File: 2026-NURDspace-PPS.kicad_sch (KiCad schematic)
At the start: 4 parts

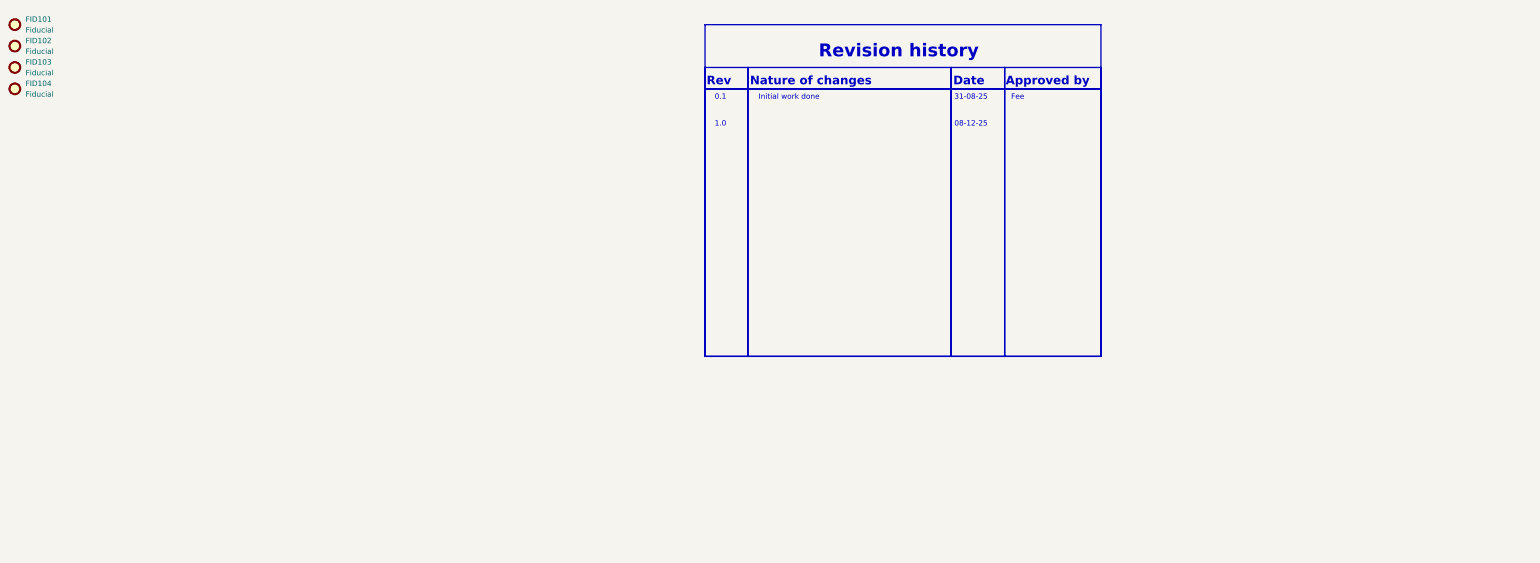
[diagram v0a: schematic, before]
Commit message: Started on gathering parts
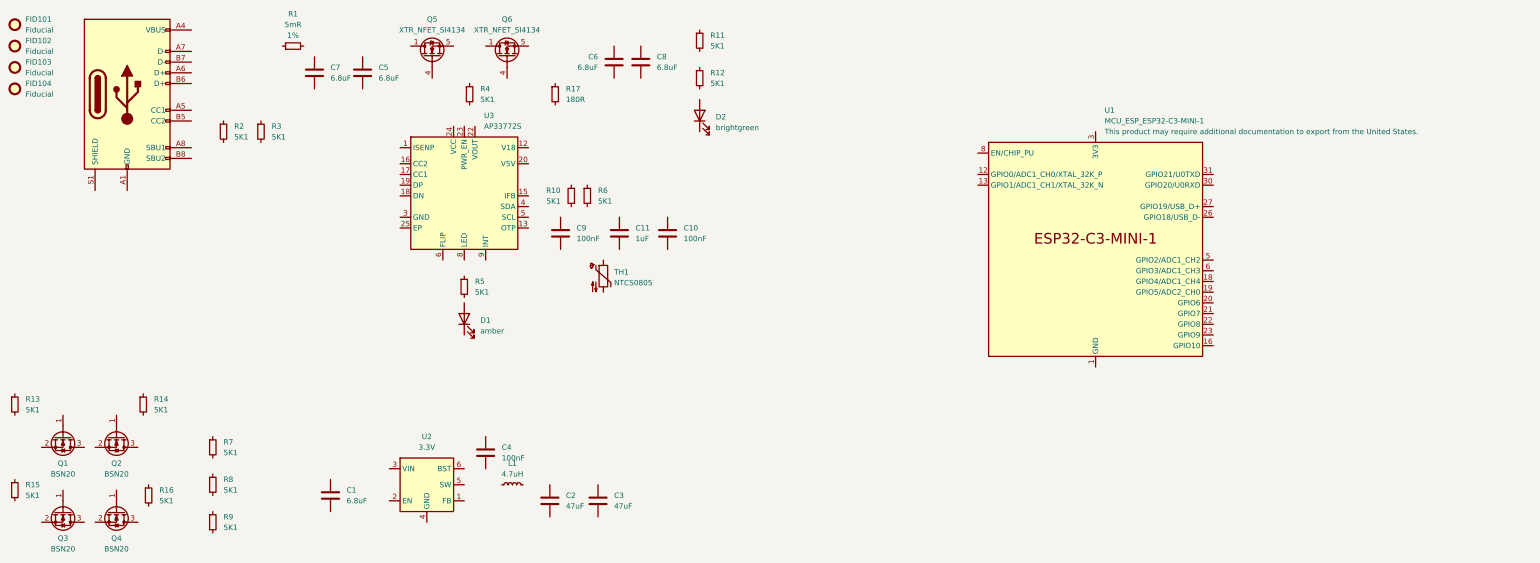
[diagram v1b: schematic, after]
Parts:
- added C1, C5, C6, C7, C8: 6.8uF, Capacitor_SMD:C_1206_3216Metric, symbol 0_NRD_Capacitors_MLCC:CB_＋＝_1206B685K500CT
- added C10, C4, C9: 100nF, Capacitor_SMD:C_0805_2012Metric, symbol 0_NRD_Capacitors_MLCC:C8_＊％_0805B104K500CT
- added C11: 1uF, Capacitor_SMD:C_1206_3216Metric, symbol 0_NRD_Capacitors_MLCC:CB_＋＃_1206B105K250CT
- added C2, C3: 47uF, Capacitor_SMD:C_1210_3225Metric, symbol 00_projectlib:CB_＝！_MAASL32MSB7476MPNA01
- added D1: amber, LED_SMD:LED_0603_1608Metric, symbol 0_NRD_Leds_and_Opto:LED_WRTH_150060AS75000
- added D2: brightgreen, LED_SMD:LED_0603_1608Metric, symbol 0_NRD_Leds_and_Opto:LED_WRTH_150060VS75000
- added J1: UJ20-C-H-C-4-SMT-TR, 0_NRD_footprints:USB_C_Receptacle_SSKY_UJ20-C-H-C-4-SMT-TR, symbol 0_NRD_Connectors:USB_SSKY_UJ20-C-H-C-4-SMT-TR
- added L1: 4.7uH, 0_NRD_footprints:FB_2020_5650Metric, symbol 00_projectlib:IND_VSHY_IMC2220ER4R7K
- added Q1, Q2, Q3, Q4: BSN20, Package_TO_SOT_SMD:SOT-23, symbol 00_projectlib:XTR_NFET_BSN20
- added Q5, Q6: XTR_NFET_SI4134, Package_SO:SOIC-8_3.9x4.9mm_P1.27mm, symbol 00_projectlib:XTR_NFET_SI4134
- added R1: 5mR, Resistor_SMD:R_1206_3216Metric, symbol 00_projectlib:RES_1206_5mR
- added R10, R11, R12, R13, R14, R15, R16, R2, R3, R4, R5, R6, R7, R8, R9: 5K1, Resistor_SMD:R_0805_2012Metric, symbol 0_NRD_Resistors:R_0805_5K1
- added R17: 180R, Resistor_SMD:R_0805_2012Metric, symbol 0_NRD_Resistors:R_0805.ͺ_180R
- added TH1: NTCS0805, Resistor_SMD:R_0805_2012Metric, symbol 00_projectlib:NTC_NTCS0805E3103HHT
- added U1: MCU_ESP_ESP32-C3-MINI-1, 0_NRD_footprints:ESP32-C3-MINI-1U, symbol 0_NRD_Microcontrollers:MCU_ESP_ESP32-C3-MINI-1U
- added U2: 3.3V, Package_TO_SOT_SMD:TSOT-23-6, symbol 00_projectlib:BCK_DIOD_AP63203
- added U3: AP33772S, Package_DFN_QFN:QFN-24-1EP_4x4mm_P0.5mm_EP2.6x2.6mm, symbol 00_projectlib:AP33772S
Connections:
- new net: Q6.1 (S), Q6.2 (S), Q6.3 (S)
- new net: Q6.5 (D), Q6.6 (D), Q6.7 (D), Q6.8 (D)
- new net: U1.1 (GND), U1.11 (GND), U1.14 (GND), U1.2 (GND), U1.36 (GND), U1.37 (GND), U1.38 (GND), U1.39 (GND), U1.40 (GND), U1.41 (GND), U1.42 (GND), U1.43 (GND), U1.44 (GND), U1.45 (GND), U1.46 (GND), U1.47 (GND), U1.48 (GND), U1.49 (GND), U1.50 (GND), U1.51 (GND), U1.52 (GND), U1.53 (GND)
- new net: U3.10 (NC), U3.11 (NC), U3.14 (NC), U3.2 (NC), U3.21 (NC), U3.7 (NC)
- new net: J1.A1 (GND), J1.A12 (GND), J1.B1 (GND), J1.B12 (GND)
- new net: J1.A4 (VBUS), J1.A9 (VBUS), J1.B4 (VBUS), J1.B9 (VBUS)
- new net: Q5.1 (S), Q5.2 (S), Q5.3 (S)
- new net: Q5.5 (D), Q5.6 (D), Q5.7 (D), Q5.8 (D)
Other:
- note removed: "0.1"
- note removed: "08-12-25"
- note removed: "1.0"
- note removed: "31-08-25"
- note removed: "Approved by"
- note removed: "Date"
- note removed: "Fee"
- note removed: "Initial work done"
- note removed: "Nature of changes"
- note removed: "Rev"
- note removed: "Revision history"

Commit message: Added all components
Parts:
- removed C2, C3: 47uF, Capacitor_SMD:C_1210_3225Metric, symbol 00_projectlib:CB_＝！_MAASL32MSB7476MPNA01
- removed L1: 4.7uH, 0_NRD_footprints:FB_2020_5650Metric, symbol 00_projectlib:IND_VSHY_IMC2220ER4R7K
- removed R1: 5mR, Resistor_SMD:R_1206_3216Metric, symbol 00_projectlib:RES_1206_5mR
- removed U1: MCU_ESP_ESP32-C3-MINI-1, 0_NRD_footprints:ESP32-C3-MINI-1U, symbol 0_NRD_Microcontrollers:MCU_ESP_ESP32-C3-MINI-1U
- added C105: 1uF, Capacitor_SMD:C_1206_3216Metric, symbol 0_NRD_Capacitors_MLCC:CB_＋＃_1206B105K250CT
- added C107: 180uF, 0_NRD_footprints:CP_Wurth_WCAP-PHLE-L7.3W4.3H1.9, symbol 00_projectlib:WCAP_WURTH_875035119002
- added C112: 100nF, Capacitor_SMD:C_0805_2012Metric, symbol 0_NRD_Capacitors_MLCC:C8_＊％_0805B104K500CT
- added D101, D102, D103, D104, D105, D106, D107, D108, D110, D111, D112, D113, D114, D115, D116, D117: MXA8-PW40-0000, 0_NRD_footprints:LED_Luxeon3535_3.5x3.7mm, symbol 00_projectlib:LED_LUML_MXA8-PW40-0000
- added D119, D120, D121, D122, D123, D124, D125, D126, D127, D128: Led_0603_superred_generic, LED_SMD:LED_0603_1608Metric, symbol 0_NRD_Leds_and_Opto:LED_WRTH_150060SS75000
- added L101: 4.7uH, Inductor_SMD:L_1008_2520Metric_Pad1.43x2.20mm_HandSolder, symbol 00_projectlib:IND_WRTH_74479889247
- added R105, R106, R107, R108, R109, R110, R111, R112, R117, R118, R119, R120, R123, R124, R125, R126: 39R, Resistor_SMD:R_0805_2012Metric, symbol 0_NRD_Resistors:R_0805.__39R
- added R122: 5mR, Resistor_SMD:R_0805_2012Metric_Pad1.20x1.40mm_HandSolder, symbol 00_projectlib:RES_0805_5mR
- added R132, R133, R134, R135, R136, R139, R140, R141, R142, R143: 270R, Resistor_SMD:R_0805_2012Metric, symbol 0_NRD_Resistors:R_0805.ͺ_270R
- added R144: 5K1, Resistor_SMD:R_0805_2012Metric, symbol 0_NRD_Resistors:R_0805_5K1
- added SW101: 430172085816, 0_NRD_footprints:btn_momentary_430172085816, symbol 0_NRD_User_Inputs:BTN_MTRY_430172085816
- added U101, U102, U103, U104, U105, U106, U108, U109, U113, U114, U115, U116, U118, U119, U121, U122: 1G126, Package_TO_SOT_SMD:SOT-353_SC-70-5, symbol 0_NRD_Level_and_logic:LOG_7400_1G126
- added U107, U112, U117, U120: 74HC595, Package_SO:SOIC-16_3.9x9.9mm_P1.27mm, symbol 0_NRD_Level_and_logic:LOG_7400_595
- added U123: 481RV12172100, 0_NRD_footprints:481RV12172100, symbol 00_projectlib:BTN_ENC_WURTH_481RV12172100
- added U124: ESP32-S3-WROOM-1, 0_NRD_footprints:ESP32-S3-WROOM-1, symbol 0_NRD_Microcontrollers:MCU_ESP_ESP32-S3-WROOM-1
- renumbered C7 to C101, C1 to C102, C5 to C103, C4 to C104, C9 to C106, C6 to C108, C11 to C109, C8 to C110, C10 to C111, D1 to D109, D2 to D118, J1 to J101, Q1 to Q101, Q3 to Q102, Q2 to Q103, Q4 to Q104, Q5 to Q105, Q6 to Q106, R13 to R101, R15 to R102, R14 to R103, R16 to R104, R7 to R113, R8 to R114, R9 to R115, R2 to R116, R3 to R121, R5 to R127, R4 to R128, R17 to R129, R10 to R130, R6 to R131, R11 to R137, R12 to R138, TH1 to TH101, U2 to U110, U3 to U111
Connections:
- new net: U124.1 (GND), U124.40 (GND), U124.41 (GND)
- new net +3.3V: R144.1
- new net ESP_BOOTSEL: C112.1, R144.2, SW101.1, SW101.2
- new net GND: C112.2, SW101.3, SW101.4
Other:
- note added: "3V to 20V indicator"
- note added: "Boot Select"
- note added: "Decimal indicator"
- note added: "Google AN97055"

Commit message: Drawn the schematic
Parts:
- removed D101, D102, D103, D104, D105, D106, D107, D108, D110, D111, D112, D113, D114, D115, D116, D117: MXA8-PW40-0000, 0_NRD_footprints:LED_Luxeon3535_3.5x3.7mm, symbol 00_projectlib:LED_LUML_MXA8-PW40-0000
- removed D119, D120, D121, D122, D123, D124, D125, D126, D127, D128: Led_0603_superred_generic, LED_SMD:LED_0603_1608Metric, symbol 0_NRD_Leds_and_Opto:LED_WRTH_150060SS75000
- removed R105, R106, R107, R108, R109, R110, R111, R112, R117, R118, R119, R120, R123, R124, R125, R126: 39R, Resistor_SMD:R_0805_2012Metric, symbol 0_NRD_Resistors:R_0805.__39R
- removed R113, R114, R130, R131: 5K1, Resistor_SMD:R_0805_2012Metric, symbol 0_NRD_Resistors:R_0805_5K1
- removed R132, R133, R134, R135, R136, R139, R140, R141, R142, R143: 270R, Resistor_SMD:R_0805_2012Metric, symbol 0_NRD_Resistors:R_0805.ͺ_270R
- removed U101, U102, U103, U104, U105, U106, U108, U109, U113, U114, U115, U116, U118, U119, U121, U122: 1G126, Package_TO_SOT_SMD:SOT-353_SC-70-5, symbol 0_NRD_Level_and_logic:LOG_7400_1G126
- removed U107, U112, U117, U120: 74HC595, Package_SO:SOIC-16_3.9x9.9mm_P1.27mm, symbol 0_NRD_Level_and_logic:LOG_7400_595
- added C108, C110, C115: 100nF, Capacitor_SMD:C_0805_2012Metric, symbol 0_NRD_Capacitors_MLCC:C8_＊％_0805B104K500CT
- added R109, R110, R112, R118: 5K1, Resistor_SMD:R_0805_2012Metric, symbol 0_NRD_Resistors:R_0805_5K1
- renumbered C103 to C102, C108 to C103, C110 to C104, C109 to C105, C112 to C107, C111 to C109, C104 to C111, C102 to C112, C105 to C113, C107 to C114, D118 to D101, D109 to D102, Q105 to Q101, Q106 to Q102, Q101 to Q103, Q103 to Q104, Q102 to Q105, Q104 to Q106, R122 to R101, R137 to R102, R138 to R103, R128 to R104, R129 to R105, R116 to R106, R121 to R107, R144 to R108, R127 to R111, R101 to R113, R103 to R114, R102 to R116, R104 to R117, U111 to U101, U124 to U102, U123 to U103, U110 to U104
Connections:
- net +3.3V: now also C113.1, C114.1, L101.2, Q104.1 (G), Q106.1 (G), R114.1, R115.1, R117.1, U102.2 (3V3), U104.1 (FB), C108.1, R109.1, R110.1, R118.1
- net ESP_BOOTSEL: now also U102.27 (GPIO0/BOOT)
- net GND: now also C101.2, C102.2, C103.2, C104.2, C105.2, C106.2, C109.2, C112.2, C113.2, C114.2, D101.1 (K), D102.1 (K), J101.A1 (GND), J101.A12 (GND), J101.B1 (GND), J101.B12 (GND), J101.S1 (SHIELD), R106.2, R107.2, TH101.2, U101.25 (EP), U101.3 (GND), U102.1 (GND), U102.40 (GND), U102.41 (GND), U103.13, U104.4 (GND), C108.2, C110.2, C115.2, R112.2
- net VBUS: now reaches C103.1
- net VBUS: now also C104.1, C112.1, Q102.5 (D), Q102.6 (D), Q102.7 (D), Q102.8 (D), R102.1, R105.1, U104.2 (EN), U104.3 (VIN)
- net at D102.2 (A): now also R111.2
- net at U103.1: now also U102.15 (GPIO3/TOUCH3/ADC1_CH2)
- net at U103.2: now also U102.4 (GPIO4/TOUCH4/ADC1_CH3)
- net at U103.3: now also U102.5 (GPIO5/TOUCH5/ADC1_CH4)
- net at U103.4: now also U102.6 (GPIO6/TOUCH6/ADC1_CH5)
- net at U103.5: now also U102.17 (GPIO9/TOUCH9/ADC1_CH8/FSPIHD/SUBSPIHD)
- net at U103.6: now also U102.18 (GPIO10/TOUCH10/ADC1_CH9/FSPICS0/FSPIIO4/SUBSPICS0)
- net at U103.7: now also U102.19 (GPIO11/TOUCH11/ADC2_CH0/FSPID/FSPIIO5/SUBSPID)
- net at U103.8: now also U102.20 (GPIO12/TOUCH12/ADC2_CH1/FSPICLK/FSPIIO6/SUBSPICLK)
- net at U103.C: now also R115.2, C115.1
- net at R103.1: now also R102.2
- net at R103.2: now also D101.2 (A)
- net at R106.1: now also J101.B5 (CC2), U101.16 (CC2)
- net at U103.12: now also U102.23 (GPIO21), R118.2
- net +5V: now reaches Q105.1 (G)
- net +5V: now also C105.1, Q103.1 (G), R113.1, R116.1, U101.20 (V5V)
- net I^{2}C_{SCL5V}: now reaches Q105.2 (S)
- net I^{2}C_{SCL5V}: now also R116.2, U101.5 (SCL)
- net at Q105.3 (D): now also Q106.2 (S)
- net DATA1: now reaches U102.11 (GPIO18/U1RXD/ADC2_CH7/CLK_OUT3)
- net CLK: now reaches U102.12 (GPIO8/TOUCH8/ADC1_CH7/SUBSPICS1)
- net D-: now reaches U102.13 (GPIO19/U1RTS/ADC2_CH8/CLK_OUT2/USB_D-)
- net D-: now also J101.A7 (D-), J101.B7 (D-)
- net D+: now reaches U102.14 (GPIO20/U1CTS/ADC2_CH9/CLK_OUT1/USB_D+)
- net D+: now also J101.A6 (D+), J101.B6 (D+)
- net at U102.21 (GPIO13/TOUCH13/ADC2_CH2/FSPIQ/FSPIIO7/SUBSPIQ): now also U103.L2
- net at U102.22 (GPIO14/TOUCH14/ADC2_CH3/FSPIWP/FSPIDQS/SUBSPIWP): now also U103.L1
- net at U102.3 (EN): now also C110.1, R109.2
- net I^{2}C_{SCL3V3}: now reaches U102.36 (U0RXD/GPIO44/CLK_OUT2)
- net I^{2}C_{SCL3V3}: now also Q106.3 (D), R117.2
- net I^{2}C_{SDA3V3}: now reaches U102.37 (U0TXD/GPIO43/CLK_OUT1)
- net I^{2}C_{SDA3V3}: now also Q104.2 (S), R114.2
- net OE: now reaches U102.38 (GPIO2/TOUCH2/ADC1_CH1)
- net OE: now also R112.1
- net ~{CLR}: now reaches U102.39 (GPIO1/TOUCH1/ADC1_CH0)
- net ~{CLR}: now also R110.2
- net at R111.1: now also U101.8 (LED)
- net at Q102.1 (S), Q102.2 (S), Q102.3 (S): now also Q101.1 (S), Q101.2 (S), Q101.3 (S)
- net at Q102.4 (G): now also Q101.4 (G), R104.1
- net I^{2}C_{SDA5V}: now reaches Q103.2 (S)
- net I^{2}C_{SDA5V}: now also R113.2, U101.4 (SDA)
- net at Q103.3 (D): now also Q104.3 (D)
- net at R107.1: now also J101.A5 (CC1), U101.17 (CC1)
- net at C106.1: now also U101.12 (V18)
- net at C101.1: now also C102.1, Q101.5 (D), Q101.6 (D), Q101.7 (D), Q101.8 (D), R101.2, U101.24 (VCC)
- net at R105.2: now also U101.22 (VOUT)
- net at R104.2: now also U101.23 (PWR_EN)
- net at L101.1: now also C111.2, U104.5 (SW)
- net at U101.1 (ISENP): now also J101.A4 (VBUS), J101.A9 (VBUS), J101.B4 (VBUS), J101.B9 (VBUS), R101.1
- net at U101.13 (OTP): now also TH101.1
- net at U101.15 (IFB): now also C109.1
- net at C111.1: now also U104.6 (BST)
- no-connect marks 0 -> 6
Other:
- added sheet Output Indicators (Output Indicators.kicad_sch)
- note removed: "3V to 20V indicator"
- note removed: "Decimal indicator"
- moved on the sheet: C101, C102, C103, C104, C105, C106, C107, C109, C111, C112, C113, C114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

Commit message: First version of layout
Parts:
- removed SW101: 430172085816, 0_NRD_footprints:btn_momentary_430172085816, symbol 0_NRD_User_Inputs:BTN_MTRY_430172085816
- added SW101: 430483025816, 0_NRD_footprints:SW_Push_430483025816, symbol 0_NRD_User_Inputs:BTN_MTRY_430483025816
- U102: renamed from U101; footprint Package_DFN_QFN:QFN-24-1EP_4x4mm_P0.5mm_EP2.6x2.6mm -> Interface_USBC:QFN-24-1EP_4x4mm_P0.5mm_EP2.6x2.6mm
- renumbered C112 to C103, C111 to C104, C113 to C106, C106 to C107, C103 to C108, C114 to C110, C104 to C111, C110 to C112, C108 to C113, C107 to C114, D102 to D101, D101 to D102, Q103 to Q101, Q105 to Q102, Q104 to Q103, Q106 to Q104, Q101 to Q105, Q102 to Q106, R113 to R101, R116 to R102, R106 to R103, R107 to R104, R114 to R105, R117 to R106, R101 to R107, R104 to R108, R111 to R109, R105 to R110, R102 to R111, R103 to R112, R109 to R113, R108 to R114, R118 to R115, R110 to R116, R112 to R117, R115 to R118, U104 to U101, U102 to U103, U103 to U104
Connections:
- net ESP_BOOTSEL: now also SW101.1, SW101.2
- net GND: now also SW101.3, SW101.4
- net I^{2}C_{SCL3V3}: now also Q104.2 (S), U103.8 (GPIO15/U0RTS/ADC2_CH4/XTAL_32K_P); no longer Q104.3 (D), U103.36 (U0RXD/GPIO44/CLK_OUT2)
- net I^{2}C_{SDA3V3}: now also U103.9 (GPIO16/U0CTS/ADC2_CH5/XTAL_32K_N); no longer U103.37 (U0TXD/GPIO43/CLK_OUT1)
- net at Q102.3 (D): now also Q104.3 (D); no longer Q104.2 (S)
- no-connect marks 6 -> 8
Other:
- moved on the sheet: C112, Q104, R113

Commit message: Added new version of artifact generator
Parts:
- added D103: amber, LED_SMD:LED_0603_1608Metric, symbol 0_NRD_Leds_and_Opto:LED_WRTH_150060AS75000
- added R119: 180R, Resistor_SMD:R_0805_2012Metric, symbol 0_NRD_Resistors:R_0805.ͺ_180R
- added R120: 5K1, Resistor_SMD:R_0805_2012Metric, symbol 0_NRD_Resistors:R_0805_5K1
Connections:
- net GND: now also D103.1 (K)
- net at U103.22 (GPIO14/TOUCH14/ADC2_CH3/FSPIWP/FSPIDQS/SUBSPIWP): now also R119.1; no longer U104.L1
- net at U102.10 (NC), U102.11 (NC), U102.14 (NC)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: no longer U102.7 (NC)
- new net: R119.2, U104.L1
- new net: D103.2 (A), R120.2
- new net: R120.1, U102.7 (GPIO)
- no-connect marks 8 -> 10
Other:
- moved on the sheet: D101, R109
